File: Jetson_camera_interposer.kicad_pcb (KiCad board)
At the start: 6 copper layers, 82.1 x 75 mm, 23 parts, among them J1 QSH-060-01-L-D-A, J10 JETSON_1V8, J11 VDD_3V3, J12 VDD_SYS, J13 VDD_CAM_FQ_HV_CAM, J14 CAM_AF_PWDN, J15 CAM_FLASH_EN, J16 JETSON_1V2, J17 VDD_IR, J18 IR_READY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

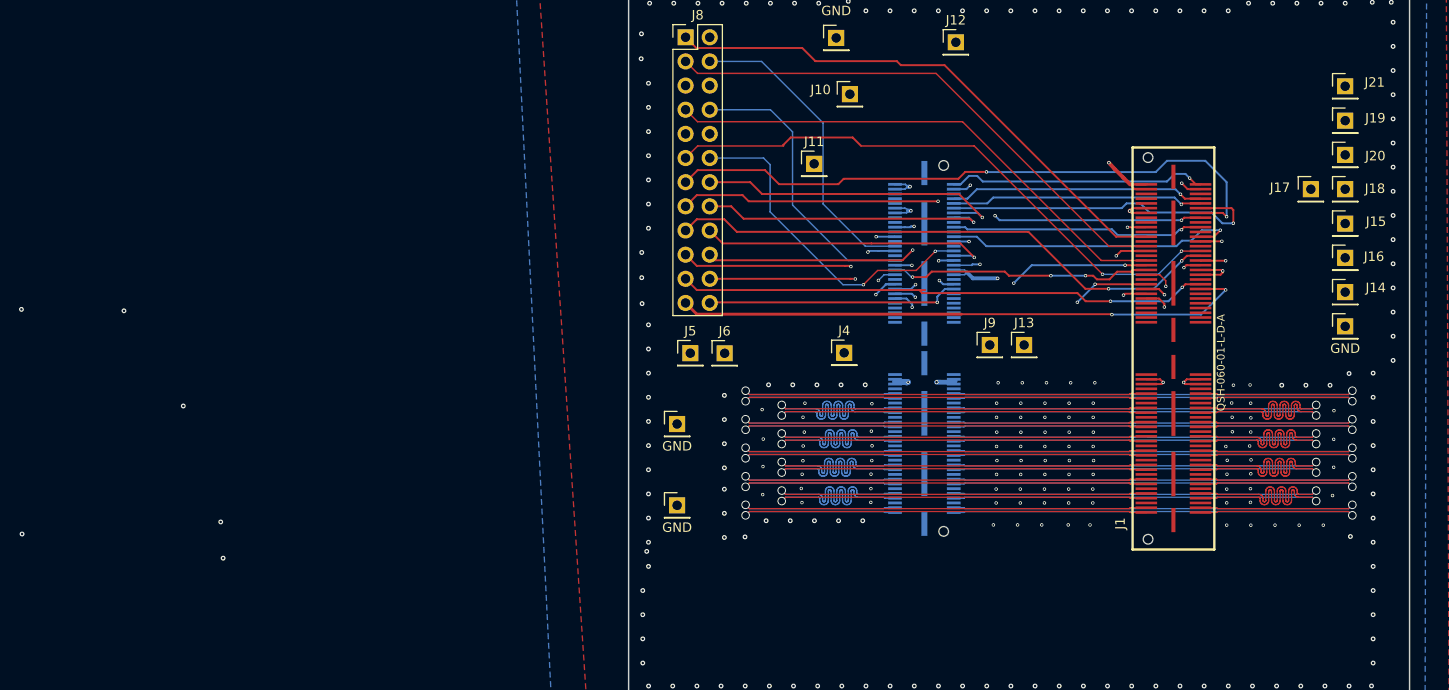
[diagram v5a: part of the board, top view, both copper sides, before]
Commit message: added stitching vias
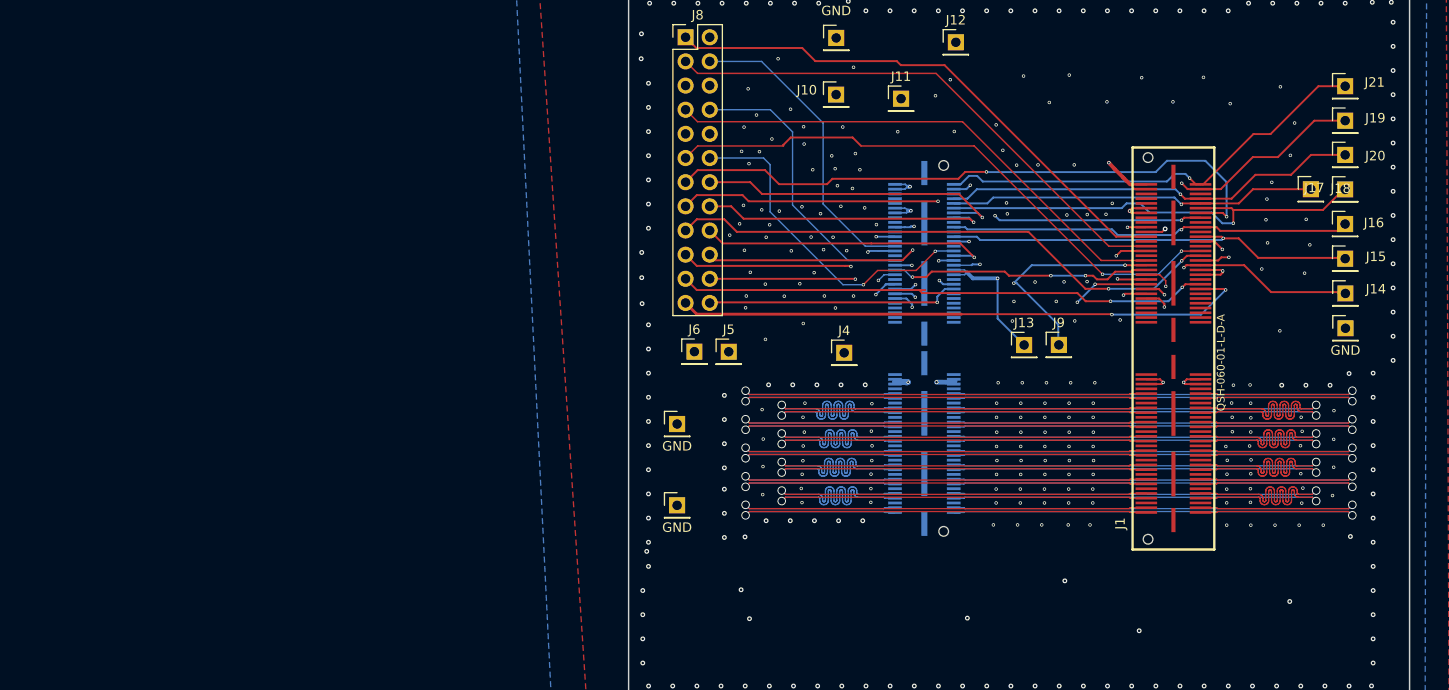
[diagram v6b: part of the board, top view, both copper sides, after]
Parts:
- moved J11 11.4 mm to (117.5, 77.2)
- moved J9 7.26 mm to (134.1, 103.1)
- moved J5 4.04 mm to (99.4, 103.8)
- moved J15 3.69 mm to (164.2, 94.1)
- moved J17 3.61 mm to (164.2, 86.8)
- moved J18 3.61 mm to (160.6, 86.8)
- moved J16 3.55 mm to (164.2, 90.4)
- moved J6 3.18 mm to (95.8, 103.8)
- moved J10 1.45 mm to (110.7, 76.8)
- moved J22 0.20 mm to (164.3, 101.4)
- moved J14 0.14 mm to (164.3, 97.7)
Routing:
- net /VDD_AF: track 27.7 -> 54.9 mm
- net /VSYS_EN: track 27.4 -> 46.8 mm
- net /JETSON_1V8: track 26.9 -> 45.1 mm
- net /CAM_INTR: track 26.8 -> 44.9 mm
- net /IR_TRIGGER: track 26.8 -> 43.9 mm
- net /CAM_AF_PWDN: track 27.4 -> 43.7 mm
- net /AVDD_CAM: track 45.7 -> 61.6 mm
- net /JETSON_1V2: track 26.6 -> 42.3 mm
- net /VDD_3V3: track 32.3 -> 46.1 mm
- net /CAM_FLASH_EN: track 31.5 -> 44.7 mm
- net /VDD_SYS: track 33.3 -> 46.3 mm
- net /VDD_IR: track 35.4 -> 48.1 mm
- net /IR_READY: track 26.6 -> 38.8 mm
- net /CAM_VSYNC: track 28.3 -> 36.9 mm
- net /VDD_CAM_FQ_HV_CAM: track 36.5 -> 44.6 mm
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
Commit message: good, before changing dimensions
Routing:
- net Earth: vias 345 -> 347

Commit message: preparing for production
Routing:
- net Earth: vias 347 -> 331
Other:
- board size 82.1 x 75 mm -> 82.1 x 67 mm
